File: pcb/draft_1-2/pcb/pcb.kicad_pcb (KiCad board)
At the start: 2 copper layers, 29.5 x 39.4 mm, 28 parts, among them J1 USB4110-GF-A, J2 SWD, U1 H3LIS200DLTR, U2 ATSAML21J16B-AUT, U3 BQ25155

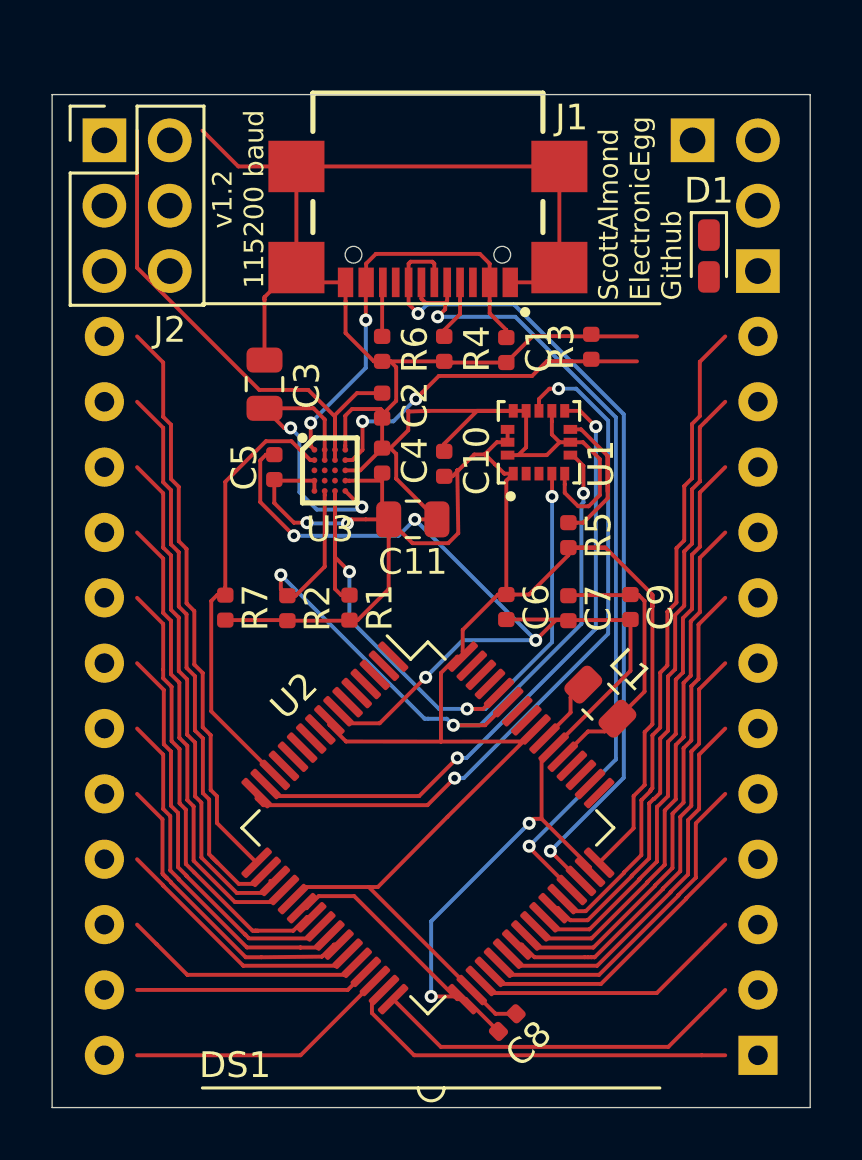
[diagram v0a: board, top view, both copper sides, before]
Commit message: add example image to readme
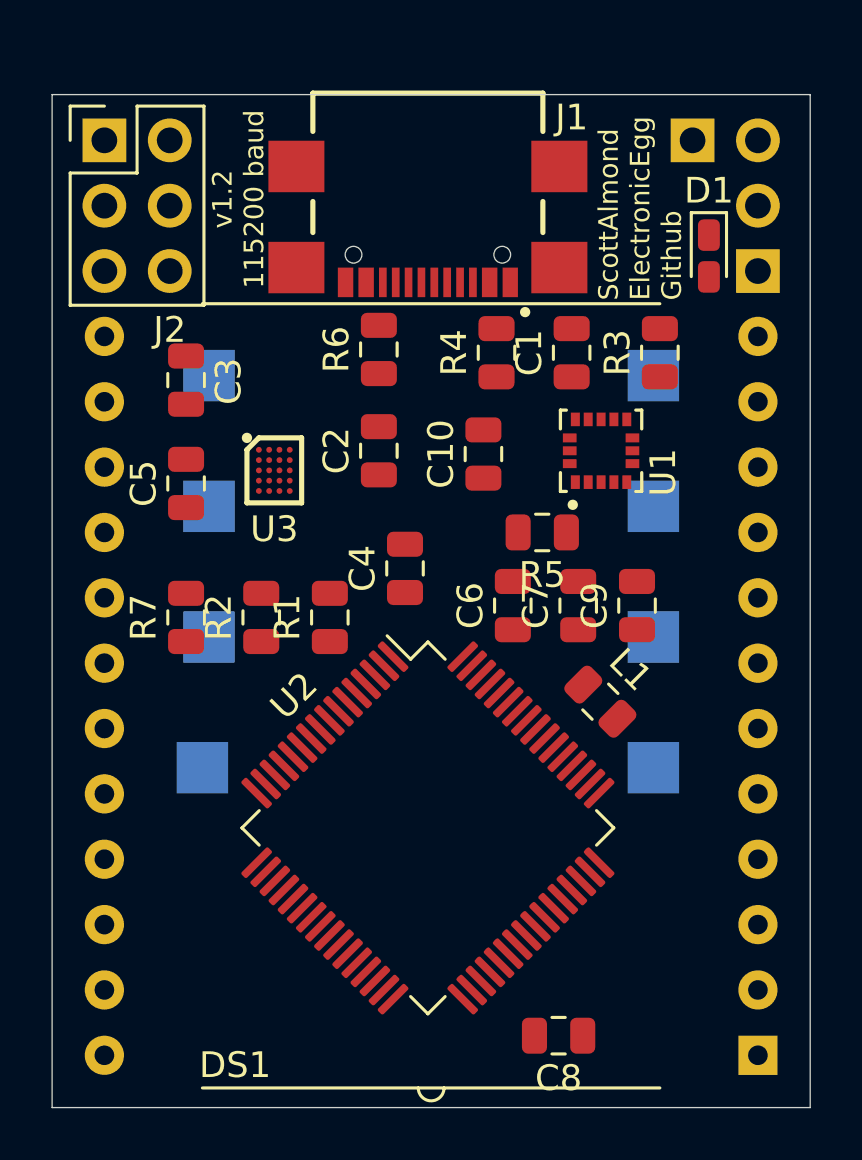
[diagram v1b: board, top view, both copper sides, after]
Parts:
- removed C11: 22uF, Capacitor_SMD:C_0805_2012Metric
- added TP1: GND, TestPoint:TestPoint_Pad_2.0x2.0mm, B.Cu at (133.1, 98.6)
- added TP2: 5V, TestPoint:TestPoint_Pad_2.0x2.0mm, B.Cu at (150.4, 98.6)
- added TP3: ~MR, TestPoint:TestPoint_Pad_2.0x2.0mm, B.Cu at (133.1, 103.6)
- added TP4: PMID, TestPoint:TestPoint_Pad_2.0x2.0mm, B.Cu at (150.4, 103.6)
- added TP5: 3V3, TestPoint:TestPoint_Pad_2.0x2.0mm, B.Cu at (150.4, 108.7)
- added TP6: 1V8, TestPoint:TestPoint_Pad_2.0x2.0mm, B.Cu at (150.4, 113.8)
- added TP7: SCL, TestPoint:TestPoint_Pad_2.0x2.0mm, B.Cu at (132.8, 113.8)
- added TP8: SDA, TestPoint:TestPoint_Pad_2.0x2.0mm, B.Cu at (133.1, 108.7)
- C1, C10, C2, C4, C5, C6, C7, C8, C9: footprint Capacitor_SMD:C_0402_1005Metric -> Capacitor_SMD:C_0805_2012Metric
- R1, R2, R3, R4, R5, R6, R7: footprint Resistor_SMD:R_0402_1005Metric -> Resistor_SMD:R_0805_2012Metric
- moved C4 4.28 mm to (140.7, 106.0)
- moved C5 3.49 mm to (132.2, 102.7)
- moved C3 3.05 mm to (132.2, 98.7)
- moved R3 2.68 mm to (150.6, 97.7)
- moved C1 2.54 mm to (147.2, 97.7), turned to 90 degrees
- moved U1 2.44 mm to (148.3, 101.5)
- moved U3 2.16 mm to (135.6, 102.2)
- moved C8 2.06 mm to (146.7, 124.2), turned to 180 degrees
- moved R4 2.04 mm to (144.3, 97.7)
- moved C2 1.76 mm to (139.7, 101.5), turned to 90 degrees
- moved C10 1.57 mm to (143.8, 101.6), turned to 90 degrees
- moved R7 1.57 mm to (132.2, 108.0), turned to 90 degrees
- moved R2 1.08 mm to (135.1, 108.0), turned to 90 degrees
- moved R5 1.02 mm to (146.1, 104.6), turned to 180 degrees
- moved R1 0.85 mm to (137.8, 108.0), turned to 90 degrees
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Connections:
- D1 pad 1: GND -> Net-(D1-Pad1)
- U2 pad 50: Net-(U2-Pad50) -> Net-(D1-Pad1)
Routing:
- net GND: track 143.5 -> 0.00 mm, vias 6 -> 0
- net +1V8: track 92.2 -> 0.00 mm, vias 2 -> 0
- net D+: track 33.6 -> 0.00 mm, vias 2 -> 0
- net D-: track 32.1 -> 0.00 mm, vias 2 -> 0
- net SDA: track 30.9 -> 0.00 mm, vias 3 -> 0
- net INT1: track 28.9 -> 0.00 mm, vias 2 -> 0
- net SCL: track 28.1 -> 0.00 mm, vias 3 -> 0
- net /1B: track 25.7 -> 0.00 mm
- net INT2: track 25.0 -> 0.00 mm, vias 2 -> 0
- net /1C: track 23.9 -> 0.00 mm
- net /1A: track 22.4 -> 0.00 mm
- net /1D: track 22.1 -> 0.00 mm
- net /1F: track 22.0 -> 0.00 mm
- net Net-(BT1-Pad1): track 20.6 -> 0.00 mm
- net /1E: track 20.3 -> 0.00 mm
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
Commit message: v1.2 draft
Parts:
- moved C6 16.9 mm to (146.2, 124.3), turned to 180 degrees
- moved C8 16.5 mm to (146.1, 107.7), turned to 270 degrees
- moved R7 5.18 mm to (133.0, 113.1), turned to 270 degrees
- moved R5 4.65 mm to (150.4, 102.9), turned to 270 degrees
- moved C7 2.97 mm to (148.2, 110.4)
- moved L1 2.79 mm to (150.4, 113.1), turned to 270 degrees
- moved R4 2.78 mm to (141.7, 98.7), turned to 180 degrees
- moved R6 2.33 mm to (137.4, 98.0), turned to 270 degrees
- moved R2 2.04 mm to (133.1, 107.7)
- moved U1 2.02 mm to (147.0, 102.9)
- moved C4 1.47 mm to (141.8, 107.1), turned to 0 degrees
- moved C2 1.45 mm to (139.8, 102.9), turned to 270 degrees
- moved C10 1.32 mm to (143.6, 102.9)
- moved C1 1.18 mm to (146.1, 98.0)
- moved C3 1.17 mm to (133.1, 98.0)
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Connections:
- U2 pad 14: INT3 -> INT1
- U2 pad 16: INT1 -> INT3
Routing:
- net GND: track 0.00 -> 184.9 mm, vias 0 -> 12
- net VREF: track 0.00 -> 94.1 mm, vias 0 -> 6
- net +3V3: track 0.00 -> 63.7 mm, vias 0 -> 2
- net SDA: track 0.00 -> 41.3 mm, vias 0 -> 1
- net D+: track 0.00 -> 38.5 mm
- net ~RESET: track 0.00 -> 38.2 mm, vias 0 -> 1
- net SWDIO: track 0.00 -> 37.7 mm, vias 0 -> 1
- net D-: track 0.00 -> 37.5 mm
- net SWCLK: track 0.00 -> 35.3 mm, vias 0 -> 1
- net +5V: track 0.00 -> 32.9 mm, vias 0 -> 2
- net Net-(C3-Pad2): track 0.00 -> 32.8 mm, vias 0 -> 3
- net SCL: track 0.00 -> 32.2 mm, vias 0 -> 1
- net Net-(D1-Pad1): track 0.00 -> 28.6 mm, vias 0 -> 2
- net Net-(R3-Pad1): track 0.00 -> 28.0 mm, vias 0 -> 1
- net Net-(D1-Pad2): track 0.00 -> 27.1 mm, vias 0 -> 2
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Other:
- board text added: "SWD v1.2 115200 baud"
- board text removed: "v1.2 115200 baud"
